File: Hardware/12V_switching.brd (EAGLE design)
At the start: 39.4 x 50.9 mm, 9 parts, among them IC5 LM2576HVSX-12/NOPB, J1 POWERPOLE_POWER45A, J2 POWERPOLE_POWER45A, J3 POWERPOLE_POWER45A

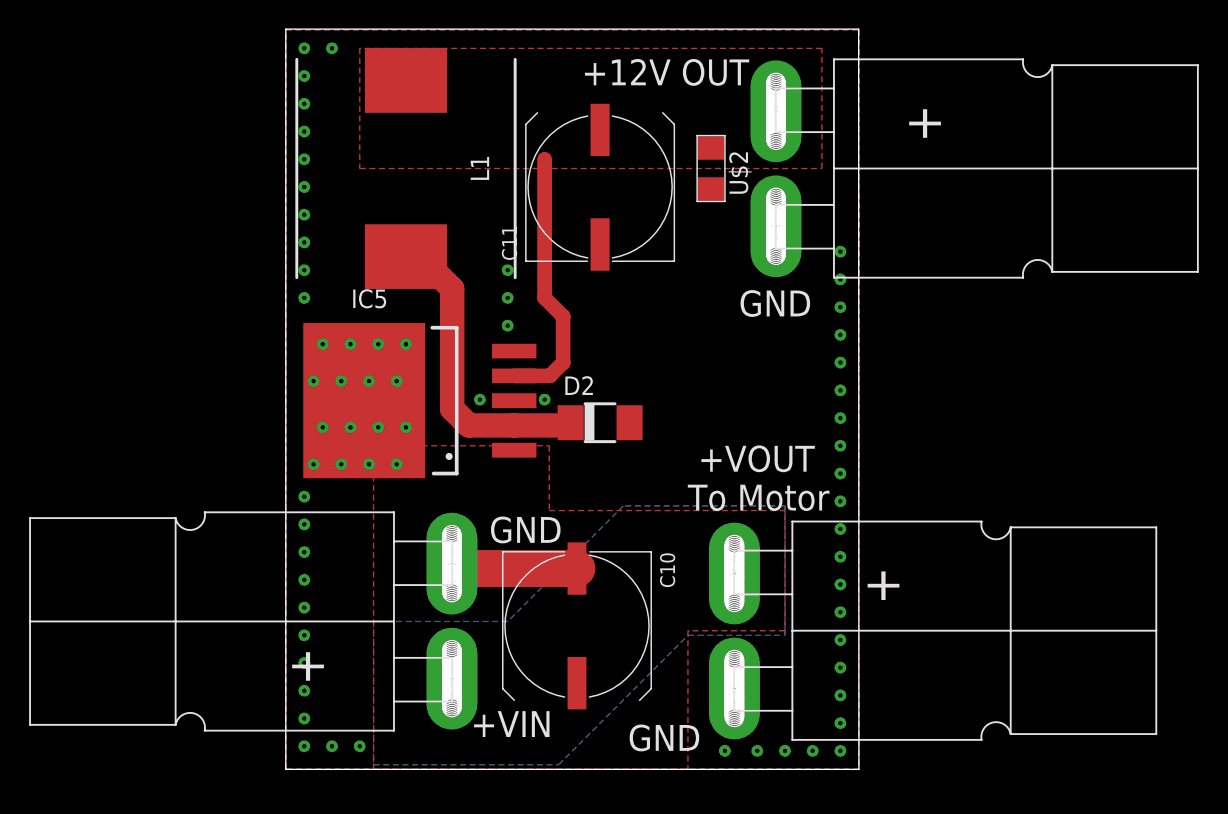
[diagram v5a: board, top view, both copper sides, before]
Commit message: Update some of the components on the 12V adapter.
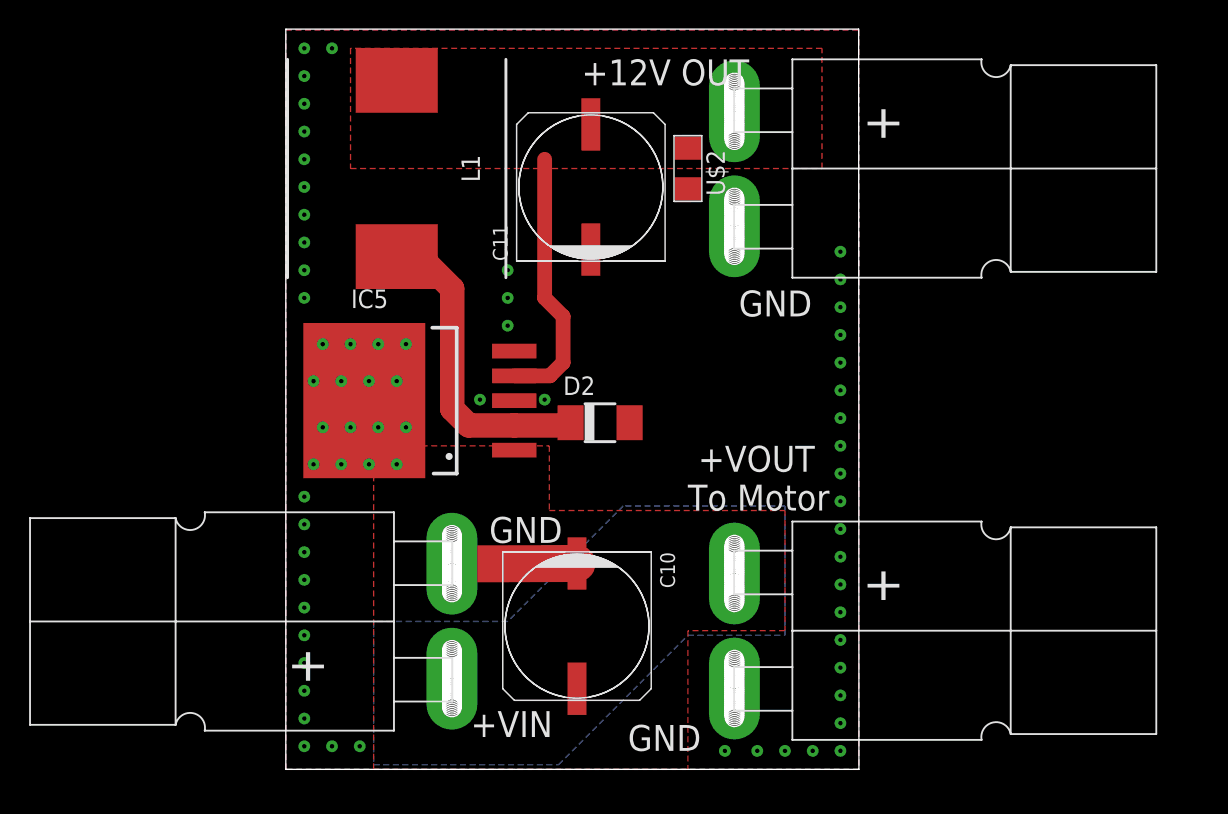
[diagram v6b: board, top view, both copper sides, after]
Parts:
- C10, C11: device rcl:UD-10X10_NICHICON -> rti:UD-10X10_NICHICON
- moved J2 2.86 mm to (30.8, 41.3)
- moved U$2 1.59 mm to (27.6, 41.3)
- moved C11 0.64 mm to (21.0, 40.0)
- moved L1 0.64 mm to (7.62, 41.3)
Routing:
- net 12VOUT: track 23.0 -> 22.4 mm
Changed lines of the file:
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@@
 <layer number="220" name="220bmp" color="21" fill="1" visible="no" active="no"/>
 <layer number="221" name="221bmp" color="22" fill="1" visible="no" active="no"/>
+<layer number="222" name="222bmp" color="23" fill="1" visible="no" active="no"/>
 <layer number="223" name="223bmp" color="24" fill="1" visible="no" active="no"/>
 <layer number="224" name="224bmp" color="25" fill="1" visible="no" active="no"/>
@@
 </autorouter>
 <elements>
-<element name="C10" library="rcl" package="UD-10X10_NICHICON" value="100uF 100V" x="20.0025" y="9.8425" rot="R270"/>
-<element name="C11" library="rcl" package="UD-10X10_NICHICON" value="1000uF" x="21.59" y="40.005" rot="R90"/>
+<element name="C10" library="rti" package="UD-10X10_NICHICON" value="100uF 100V" x="20.0025" y="9.8425" rot="R270"/>
+<element name="C11" library="rti" package="UD-10X10_NICHICON" value="1000uF" x="20.955" y="40.005" rot="R90"/>
 <element name="D2" library="diode" package="DO-214AC" value="SAC34" x="21.59" y="23.8125"/>
 <element name="IC5" library="LM2576" package="TO263-5" value="LM2576HVSX-12/NOPB" x="6.985" y="25.4" rot="R90">
@@
 <attribute name="MPN" value=" LM2576HVSX-12/NOPB" x="6.985" y="25.4" size="1.778" layer="27" rot="R90" display="off"/>
 </element>
-<element name="L1" library="MSS1583-104KEB" package="INDPM150150X860N" value="MSS1583-104KEB" x="8.255" y="41.275" rot="R90">
-<attribute name="MOUSER_PART_NUMBER" value="994-MSS1583-104KEB" x="8.255" y="41.275" size="1.778" layer="27" rot="R90" display="off"/>
-<attribute name="MANUFACTURER_NAME" value="COILCRAFT" x="8.255" y="41.275" size="1.778" layer="27" rot="R90" display="off"/>
-<attribute name="MOUSER_PRICE-STOCK" value="https://www.mouser.com/Search/Refine.aspx?Keyword=994-MSS1583-104KEB" x="8.255" y="41.275" size="1.778" layer="27" rot="R90" display="off"/>
-<attribute name="HEIGHT" value="8.6mm" x="8.255" y="41.275" size="1.778" layer="27" rot="R90" display="off"/>
-<attribute name="MANUFACTURER_PART_NUMBER" value="MSS1583-104KEB" x="8.255" y="41.275" size="1.778" layer="27" rot="R90" display="off"/>
-<attribute name="DESCRIPTION" value="Fixed Inductors MSS1583 SMT Power 0.103Ohms 100uH" x="8.255" y="41.275" size="1.778" layer="27" rot="R90" display="off"/>
+<element name="L1" library="MSS1583-104KEB" package="INDPM150150X860N" value="MSS1583-104KEB" x="7.62" y="41.275" rot="R90">
+<attribute name="MOUSER_PART_NUMBER" value="994-MSS1583-104KEB" x="7.62" y="41.275" size="1.778" layer="27" rot="R90" display="off"/>
+<attribute name="MANUFACTURER_NAME" value="COILCRAFT" x="7.62" y="41.275" size="1.778" layer="27" rot="R90" display="off"/>
+<attribute name="MOUSER_PRICE-STOCK" value="https://www.mouser.com/Search/Refine.aspx?Keyword=994-MSS1583-104KEB" x="7.62" y="41.275" size="1.778" layer="27" rot="R90" display="off"/>
+<attribute name="HEIGHT" value="8.6mm" x="7.62" y="41.275" size="1.778" layer="27" rot="R90" display="off"/>
+<attribute name="MANUFACTURER_PART_NUMBER" value="MSS1583-104KEB" x="7.62" y="41.275" size="1.778" layer="27" rot="R90" display="off"/>
+<attribute name="DESCRIPTION" value="Fixed Inductors MSS1583 SMT Power 0.103Ohms 100uH" x="7.62" y="41.275" size="1.778" layer="27" rot="R90" display="off"/>
 </element>
-<element name="U$2" library="rti" package="C1206" value="47uF" x="29.21" y="41.275" rot="R270"/>
+<element name="U$2" library="rti" package="C1206" value="47uF" x="27.6225" y="41.275" rot="R270"/>
 <element name="J1" library="powerpoles" package="POWERPOLE_PAIR_45A" value="POWERPOLE_POWER45A" x="11.43" y="10.16" rot="R90"/>
-<element name="J2" library="powerpoles" package="POWERPOLE_PAIR_45A" value="POWERPOLE_POWER45A" x="33.655" y="41.275" rot="R270"/>
+<element name="J2" library="powerpoles" package="POWERPOLE_PAIR_45A" value="POWERPOLE_POWER45A" x="30.7975" y="41.275" rot="R270"/>
 <element name="J3" library="powerpoles" package="POWERPOLE_PAIR_45A" value="POWERPOLE_POWER45A" x="30.7975" y="9.525" rot="R270"/>
 </elements>
@@
 <via x="34.29" y="1.27" extent="1-16" drill="0.3" diameter="0.8128"/>
 <contactref element="J3" pad="BLACK"/>
-<wire x1="20.0025" y1="13.7925" x2="11.41" y2="13.7925" width="2.54" layer="1"/>
-<wire x1="11.41" y1="13.7925" x2="11.41" y2="14.13" width="2.54" layer="1"/>
+<wire x1="20.0025" y1="14.1425" x2="11.41" y2="14.11" width="2.54" layer="1"/>
+<wire x1="11.41" y1="14.11" x2="11.41" y2="14.13" width="2.54" layer="1"/>
 <via x="1.27" y="18.7325" extent="1-16" drill="0.3" diameter="0.8128"/>
 <via x="1.27" y="16.8275" extent="1-16" drill="0.3" diameter="0.8128"/>
@@
 <contactref element="C11" pad="+"/>
 <polygon width="0.4064" layer="1" thermals="no">
-<vertex x="5.08" y="41.275"/>
+<vertex x="4.445" y="41.275"/>
 <vertex x="36.83" y="41.275"/>
 <vertex x="36.83" y="49.53"/>
-<vertex x="5.08" y="49.53"/>
+<vertex x="4.445" y="49.53"/>
 </polygon>
 <wire x1="15.695" y1="27.032" x2="18.142" y2="27.032" width="1.016" layer="1"/>
@@
 <wire x1="11.43" y1="33.02" x2="9.525" y2="34.925" width="1.6764" layer="1"/>
 <wire x1="9.525" y1="34.925" x2="7.285" y2="34.925" width="1.6764" layer="1"/>
-<wire x1="7.285" y1="34.925" x2="8.255" y2="35.225" width="1.6764" layer="1"/>
+<wire x1="7.285" y1="34.925" x2="7.62" y2="35.225" width="1.6764" layer="1"/>
 <wire x1="15.695" y1="23.628" x2="19.565" y2="23.628" width="1.6764" layer="1"/>
 <wire x1="19.565" y1="23.628" x2="19.565" y2="23.8125" width="1.6764" layer="1"/>
